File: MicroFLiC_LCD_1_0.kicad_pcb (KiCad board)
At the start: 2 copper layers, 14 parts, among them P1 CONN_01X01, P2 CONN_01X01, P3 CONN_01X16, Q1 BCX54-16, U1 MCP4728, U2 TLV2371

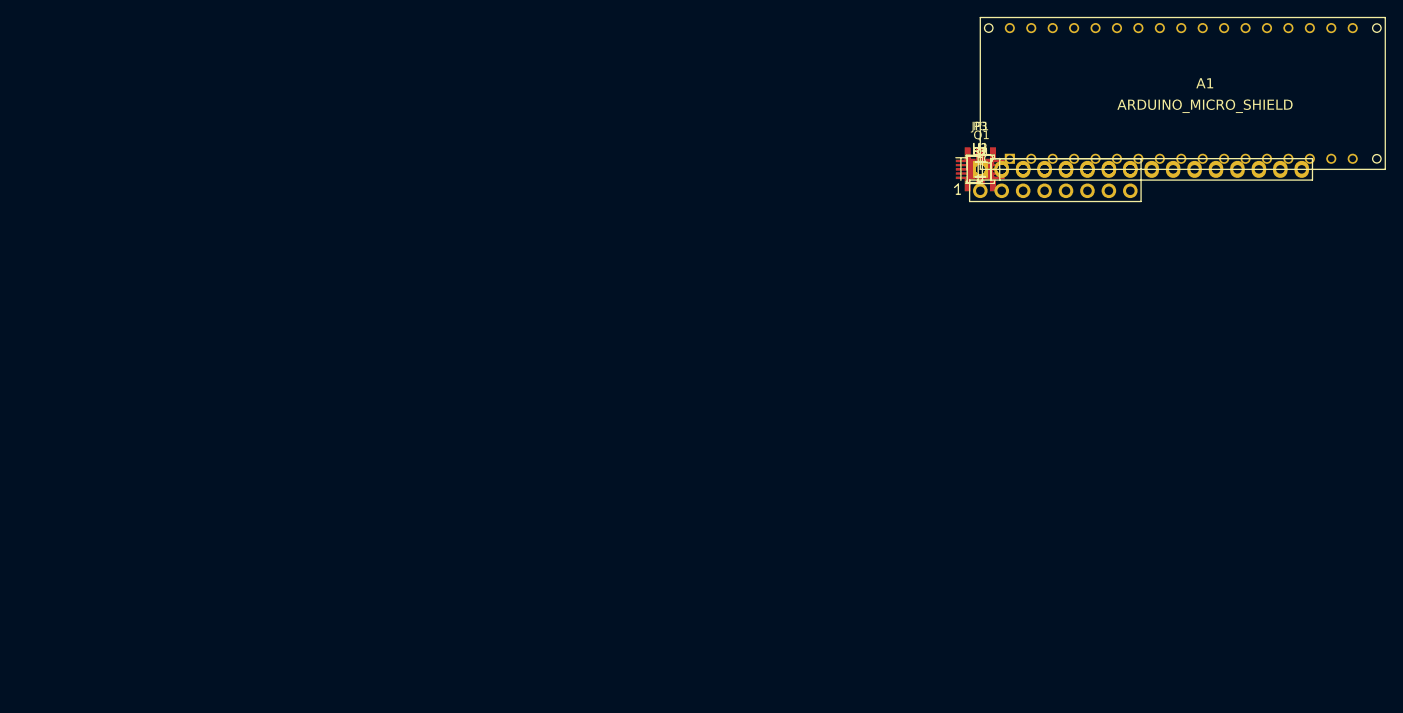
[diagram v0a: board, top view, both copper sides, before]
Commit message: Created the PCB with 3D models
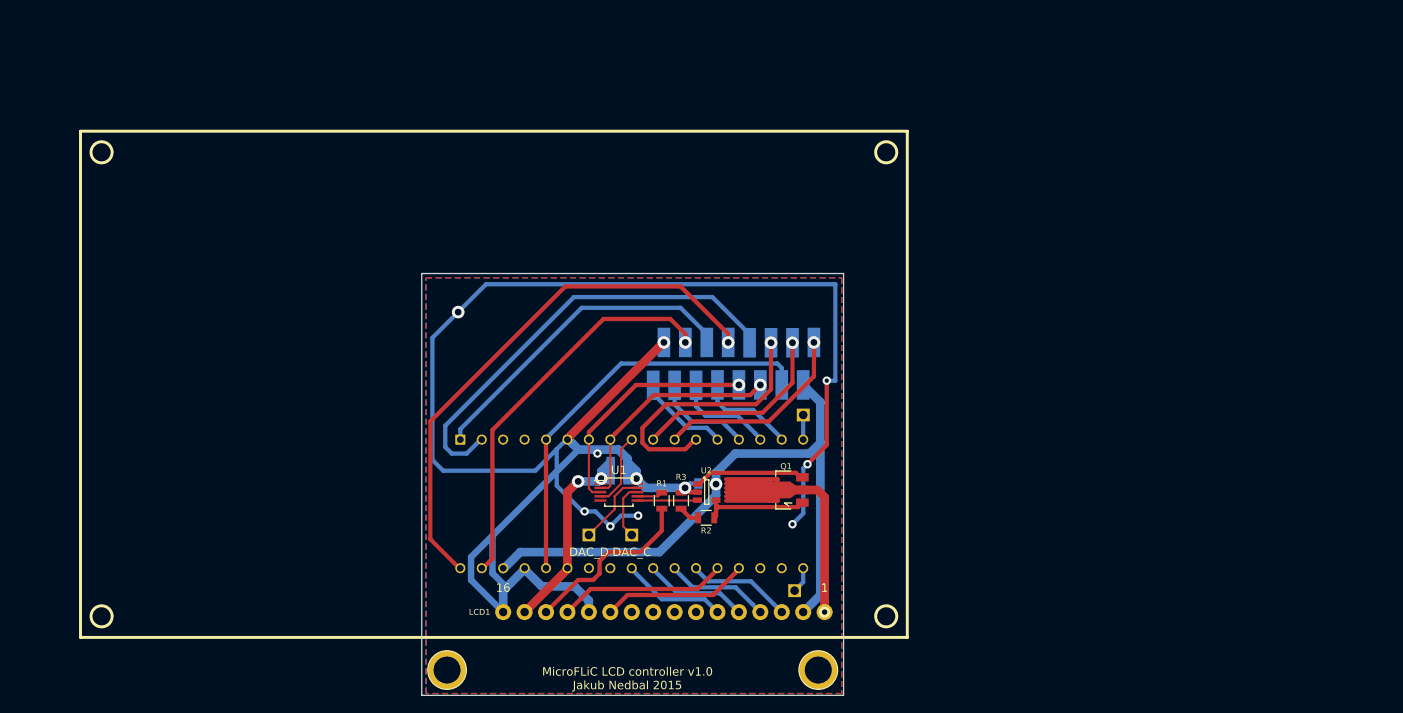
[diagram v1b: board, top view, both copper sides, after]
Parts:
- added LCD1: LCD2004, jakub:LCD2004, F.Cu at (90.8, 130.5)
- added P4: CONN_01X01, jakub:PIN_ARRAY_1, F.Cu at (126.5, 154.9)
- added REF**: 1pin, Connect:1pin, F.Cu at (129.3, 164.3)
- added REF**: 1pin, Connect:1pin, F.Cu at (85.3, 164.3)
- A1: value ARDUINO_MICRO_SHIELD -> Arduino Micro; footprint jakub:ARDUINO_MICRO_SHIELD -> jakub:ArduinoMicro; moved to B.Cu
- C1, C2, C3: moved to B.Cu
- JP1: footprint Socket_Strips:Socket_Strip_Straight_2x08 -> jakub:1-188275-6; moved to B.Cu
- P3: value CONN_01X16 -> CONN_01X01; footprint Socket_Strips:Socket_Strip_Straight_1x16 -> jakub:PIN_ARRAY_1
- Q1: footprint TO_SOT_Packages_SMD:SOT89-5_Housing -> TO_SOT_Packages_SMD:SOT89-3_Housing
- moved A1 72.0 mm to (83.4, 135.7)
- moved P3 63.5 mm to (102.1, 148.3)
- moved P2 59.9 mm to (107.2, 148.3)
- moved U1 57.4 mm to (105.7, 143.3)
- moved C2 56.4 mm to (105.7, 141.7)
- moved C1 55.1 mm to (105.7, 139.7)
- moved R1 54.5 mm to (110.7, 144.3), turned to 90 degrees
- moved R3 52.9 mm to (113.0, 144.3), turned to 90 degrees
- moved R2 52.5 mm to (116.0, 146.3), turned to 180 degrees
- moved U2 50.1 mm to (116.1, 143.3)
- moved C3 49.4 mm to (116.1, 142.2), turned to 180 degrees
- moved Q1 44.4 mm to (125.6, 143.0), turned to 90 degrees
- moved JP1 37.2 mm to (119.3, 128.1), turned to 180 degrees
- moved P1 35.9 mm to (127.5, 134.1)
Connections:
- A1 pad 12: Net-(A1-Pad12) -> /D12
- A1 pad 13: Net-(A1-Pad13) -> /D13
- A1 pad 5: /A0 -> /A1
- A1 pad 6: /A1 -> /A0
- A1 pad A0: /LCD_RS -> /LCD_E
- A1 pad A1: /LCD_E -> /LCD_RS
- A1 pad A2: /LCD_D4 -> /LCD_D7
- A1 pad A3: /LCD_D5 -> /LCD_D6
- A1 pad A4: /LCD_D6 -> /LCD_D5
- A1 pad A5: /LCD_D7 -> /LCD_D4
- A1 pad RST: Net-(A1-PadRST) -> /RST
- P1 pad 1: /DAC_C -> /D12
- P2 pad 1: /DAC_D -> /DAC_C
- P3 pad 1: /LCD_BKL -> /DAC_D
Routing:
- net GND: track 0.00 -> 226.2 mm, vias 0 -> 11
- net +12V: track 0.00 -> 74.0 mm, vias 0 -> 1
- net /D1: track 0.00 -> 64.3 mm, vias 0 -> 1
- net /LCD_BKL: track 0.00 -> 58.4 mm
- net /D0: track 0.00 -> 53.1 mm
- net /RST: track 0.00 -> 49.3 mm
- net /D3: track 0.00 -> 47.1 mm, vias 0 -> 1
- net /D2: track 0.00 -> 38.6 mm
- net /~CS: track 0.00 -> 31.6 mm, vias 0 -> 1
- net /SDA: track 0.00 -> 29.3 mm, vias 0 -> 1
- net /SCL: track 0.00 -> 27.3 mm, vias 0 -> 1
- net +5V: track 0.00 -> 27.3 mm, vias 0 -> 2
- net /A1: track 0.00 -> 24.0 mm, vias 0 -> 1
- net /A0: track 0.00 -> 23.6 mm, vias 0 -> 1
- net /LCD_CONT: track 0.00 -> 21.2 mm
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- added copper zone on B.Cu, net GND
- added copper zone on F.Cu, net GND
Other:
- board outline added: 50 x 50 mm
- net class Default: trace_width 0.25 -> 0.254
- board text added: "D12"
- board text added: "D13"
- board text added: "DAC_C"
- board text added: "DAC_D"
- board text added: "MicroFLiC LCD controller v1.0 Jakub Nedbal 2015"

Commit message: Final production board v1.0. Corrected LCD part v1.1
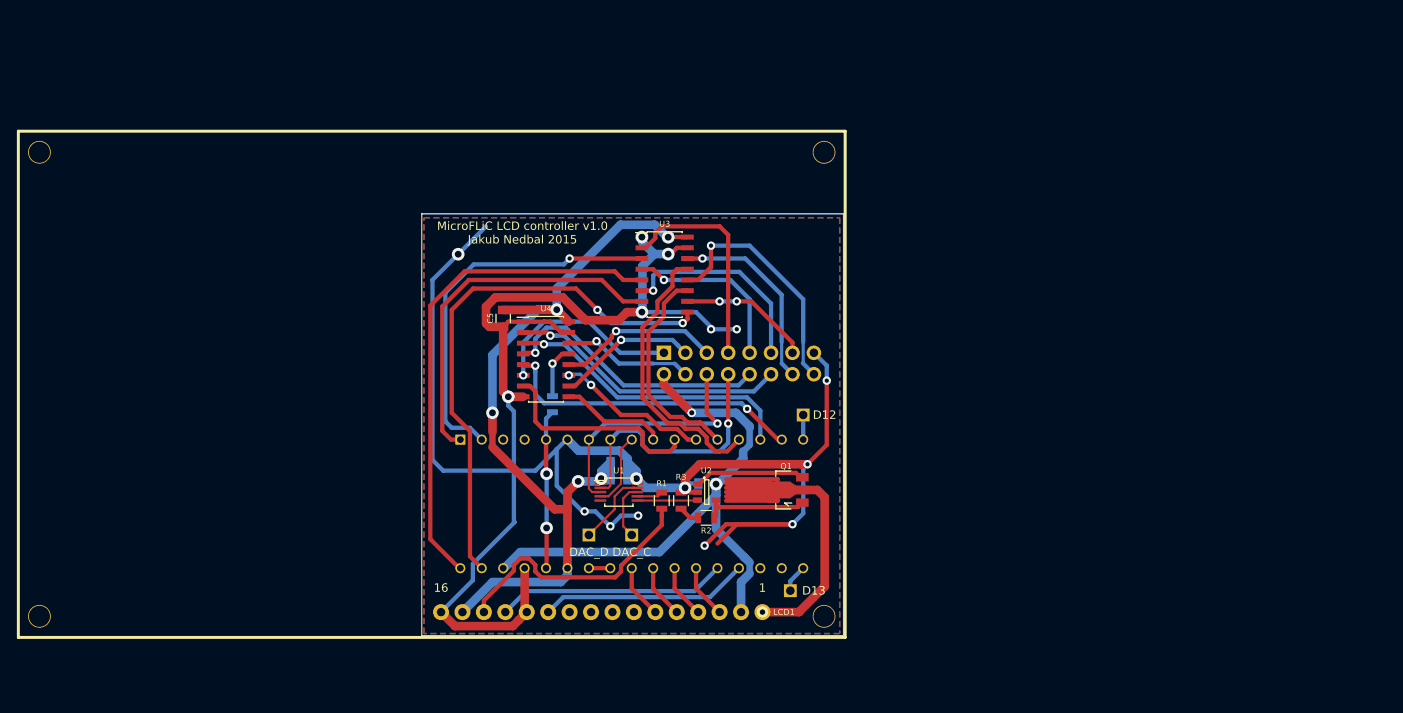
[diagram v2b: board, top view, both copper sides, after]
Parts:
- removed JP1: CONN_02X08, jakub:1-188275-6
- removed REF** (x2): 1pin, Connect:1pin
- added C4: C, Capacitors_SMD:C_0805, B.Cu at (111.5, 114.0)
- added C5: C, Capacitors_SMD:C_0805, F.Cu at (91.9, 122.7)
- added P1: CONN_02X08, Pin_Headers:Pin_Header_Straight_2x08, B.Cu at (111.0, 126.7)
- added R4: 1K5, Resistors_SMD:R_0805, B.Cu at (97.8, 132.8)
- added U3: 74AHCT367, Housings_SOIC:SOIC-16_3.9x9.9mm_Pitch1.27mm, F.Cu at (111.1, 117.5)
- added U4: 74AHCT367, Housings_SOIC:SOIC-16_3.9x9.9mm_Pitch1.27mm, F.Cu at (97.0, 127.5)
- moved LCD1 7.37 mm to (83.5, 130.5)
- moved PP4 0.51 mm to (126.0, 154.9)
- renumbered P1 to PP1, P2 to PP2, P3 to PP3, P4 to PP4
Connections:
- A1 pad 10: /D6 -> /3V3to5V/D6_5V
- A1 pad 11: /D7 -> /3V3to5V/D7_5V
- A1 pad 3.3V: Net-(A1-Pad3.3V) -> (no net)
- A1 pad 5: /A1 -> /3V3to5V/A1_5V
- A1 pad 6: /A0 -> /3V3to5V/A0_5V
- A1 pad 7: /~CS -> /3V3to5V/~CS_5V
- A1 pad 8: /D4 -> /3V3to5V/D4_5V
- A1 pad 9: /D5 -> /3V3to5V/D5_5V
- A1 pad AREF: Net-(A1-PadAREF) -> (no net)
- A1 pad MI: /D3 -> /3V3to5V/D3_5V
- A1 pad MO: /D2 -> /3V3to5V/D2_5V
- A1 pad RST: /RST -> /3V3to5V/~RST_5V
- A1 pad RX: Net-(A1-PadRX) -> (no net)
- A1 pad SCK: /D1 -> /3V3to5V/D1_5V
- A1 pad SS: /D0 -> /3V3to5V/D0_5V
- A1 pad TX: Net-(A1-PadTX) -> (no net)
- LCD1 pad 10: Net-(LCD1-Pad10) -> (no net)
- LCD1 pad 7: Net-(LCD1-Pad7) -> (no net)
- LCD1 pad 8: Net-(LCD1-Pad8) -> (no net)
- LCD1 pad 9: Net-(LCD1-Pad9) -> (no net)
- U1 pad 5: Net-(U1-Pad5) -> (no net)
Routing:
- net +5V: track 27.3 -> 97.9 mm, vias 2 -> 5
- net /D1: track 64.3 -> 0.00 mm, vias 1 -> 0
- net /3V3to5V/D3_5V: track 0.00 -> 63.8 mm, vias 0 -> 2
- net /3V3to5V/D1_5V: track 0.00 -> 59.9 mm
- net /D0: track 53.1 -> 0.00 mm
- net /RST: track 49.3 -> 0.00 mm
- net /D3: track 47.1 -> 0.00 mm, vias 1 -> 0
- net /3V3to5V/D0_5V: track 0.00 -> 45.4 mm, vias 0 -> 1
- net /3V3to5V/D2_5V: track 0.00 -> 43.3 mm
- net GND: track 226.2 -> 268.7 mm, vias 11 -> 16
- net /D2: track 38.6 -> 0.00 mm
- net /3V3to5V/D7_5V: track 0.00 -> 36.4 mm, vias 0 -> 2
- net /3V3to5V/D6_5V: track 0.00 -> 34.8 mm, vias 0 -> 1
- net /3V3to5V/D5_5V: track 0.00 -> 33.2 mm
- net /3V3to5V/D6: track 0.00 -> 33.1 mm, vias 0 -> 1
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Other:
- board text added: "+12V"
- board text added: "+5V"
- board text added: "3V3"
- board text added: "A0"
- board text added: "A0_5V"
- board text added: "A1"
- board text added: "A1_5V"
- board text added: "AREF"
- board text added: "D0"
- board text added: "D0_5V"
- board text added: "D1"
- board text added: "D1_5V"
- board text added: "D2"
- board text added: "D2_5V"
- board text added: "D3"
- board text added: "D3_5V"
- board text added: "D4"
- board text added: "D4_5V"
- board text added: "D5"
- board text added: "D5_5V"
- board text added: "D6"
- board text added: "D6_5V"
- board text added: "D7"
- board text added: "D7_5V"
- board text added: "GND"
- board text added: "LCD_BLK"
- board text added: "LCD_CONT"
- board text added: "LCD_D4"
- board text added: "LCD_D5"
- board text added: "LCD_D6"
- board text added: "LCD_D7"
- board text added: "LCD_E"
- board text added: "LCD_R/~W"
- board text added: "LCD_RS"
- board text added: "RX"
- board text added: "SCL"
- board text added: "SDA"
- board text added: "TX"
- board text added: "~CS"
- board text added: "~CS_5V"
- board text added: "~LDAC"
- board text added: "~RST"
- board text added: "~RST_5V"
